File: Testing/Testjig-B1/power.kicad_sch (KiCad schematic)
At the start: 29 parts, among them U1 LM7805_TO220, U2 LM7815_TO220, U3 LM317_TO-220, U4 LM7915_TO220, U5 LM7924_TO220

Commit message: More PSU work
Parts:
- added F1, F2, F3, F5: 100mAT, symbol Device:Fuse
- added F4: 150mAT, symbol Device:Fuse
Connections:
- net +VDC: now also F1.1, F2.1, F3.1; no longer C1.1, C2.1, C3.1, D1.1 (K), D2.1 (K), D3.1 (K), U1.1 (VI), U2.1 (VI), U3.3 (VI)
- net -VDC: now also F4.1, F5.1; no longer C4.2, C5.2, D4.2 (A), D5.2 (A), U4.2 (VI), U5.2 (VI)
- net +6V: now reaches C7.1, D1.2 (A), D11.1 (K), D6.1 (K), R2.1, U3.2 (VO)
- net +5V: now reaches C8.1, D2.2 (A), D7.1 (K), U1.3 (VO)
- net +15V: now reaches C9.1, D3.2 (A), D8.1 (K), U2.3 (VO)
- net -15V: now reaches C10.2, D4.1 (K), D9.2 (A), U4.3 (VO)
- net -24V: now reaches C11.2, D10.2 (A), D5.1 (K), U5.3 (VO)
- new net: C2.1, D2.1 (K), F2.2, U1.1 (VI)
- new net: C1.1, D1.1 (K), F1.2, U3.3 (VI)
- new net: C3.1, D3.1 (K), F3.2, U2.1 (VI)
- new net: C5.2, D5.2 (A), F5.2, U5.2 (VI)
- new net: C4.2, D4.2 (A), F4.2, U4.2 (VI)

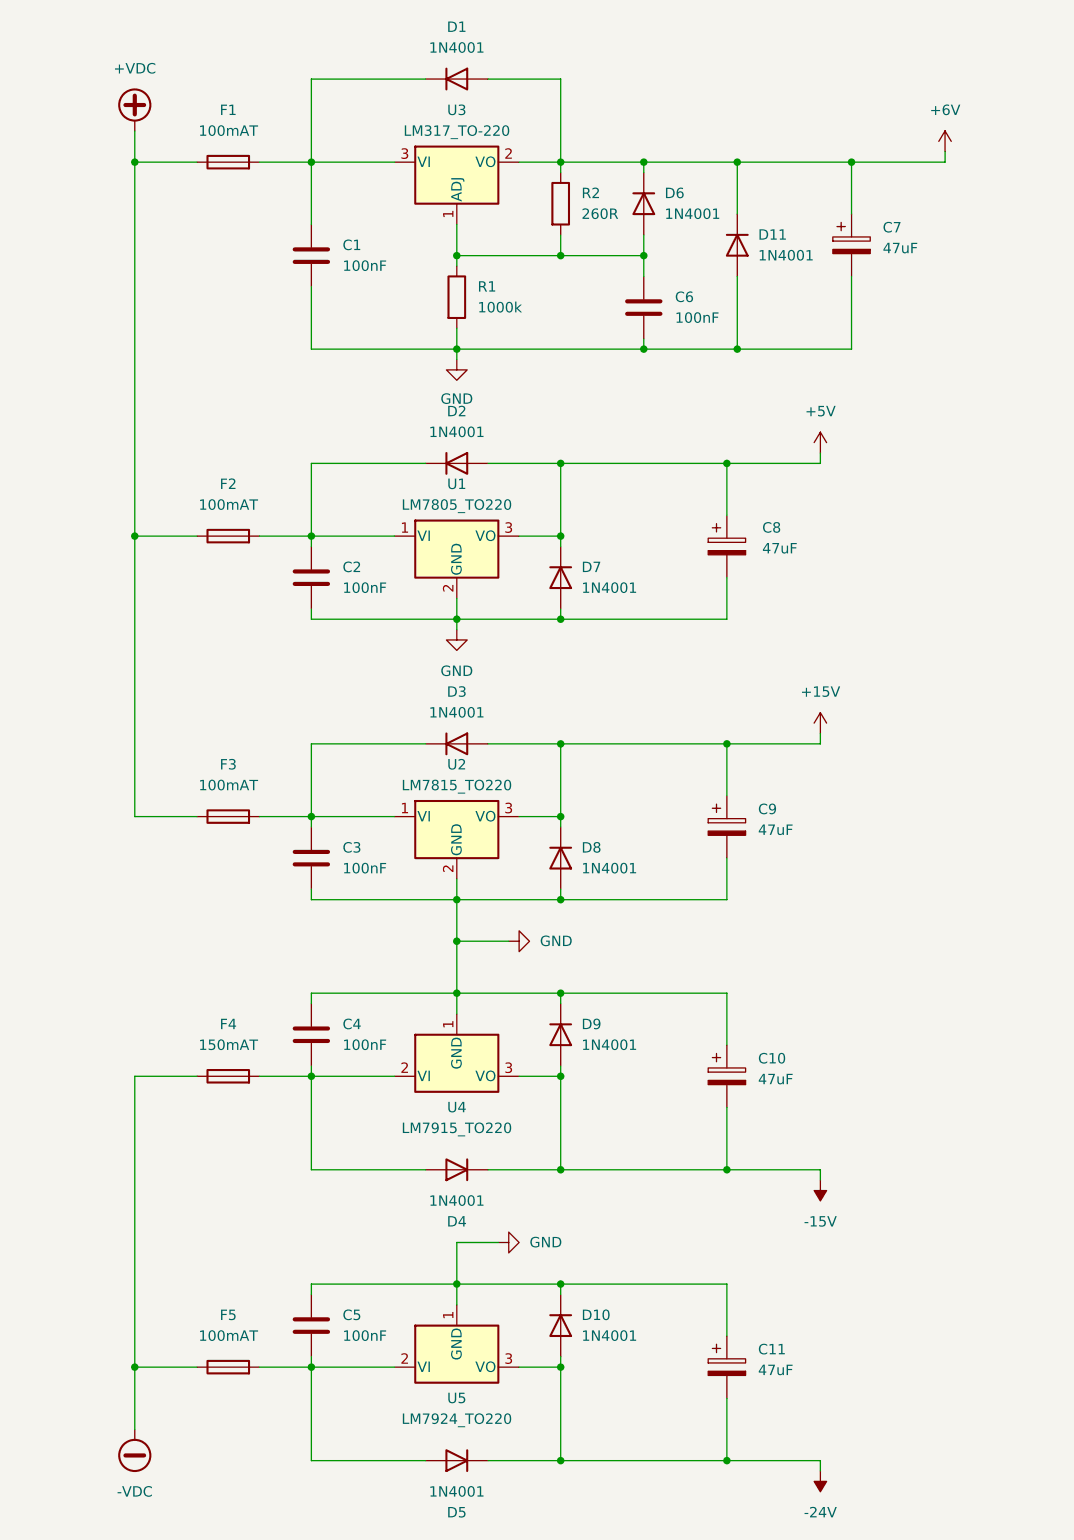
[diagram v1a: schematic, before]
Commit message: First iteration tester design
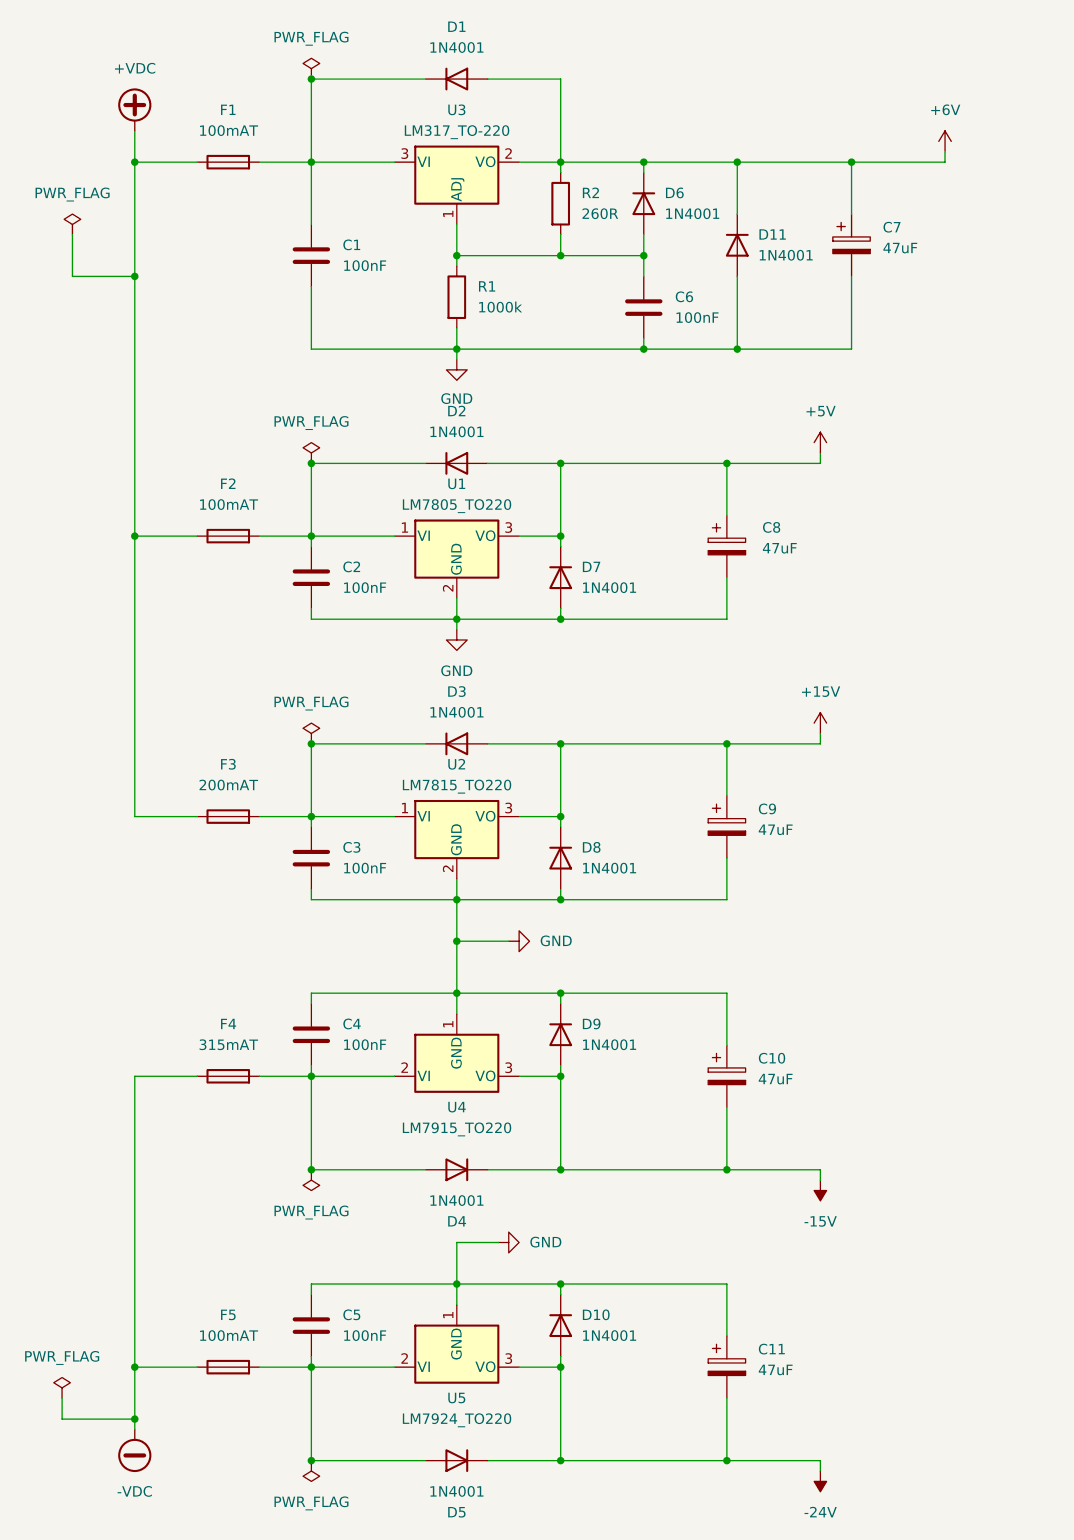
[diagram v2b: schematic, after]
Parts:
- C1, C2, C3, C4, C5, C6: footprint (none) -> Capacitor_SMD:C_0805_2012Metric_Pad1.18x1.45mm_HandSolder
- C10, C11, C7, C8, C9: footprint (none) -> Capacitor_THT:CP_Radial_D6.3mm_P2.50mm
- F1, F2, F5: footprint (none) -> Fuse:Fuseholder_Cylinder-5x20mm_Schurter_0031_8201_Horizontal_Open
- F3: value 100mAT -> 200mAT; footprint (none) -> Fuse:Fuseholder_Cylinder-5x20mm_Schurter_0031_8201_Horizontal_Open
- F4: value 150mAT -> 315mAT; footprint (none) -> Fuse:Fuseholder_Cylinder-5x20mm_Schurter_0031_8201_Horizontal_Open
- R1, R2: footprint (none) -> Resistor_SMD:R_0805_2012Metric

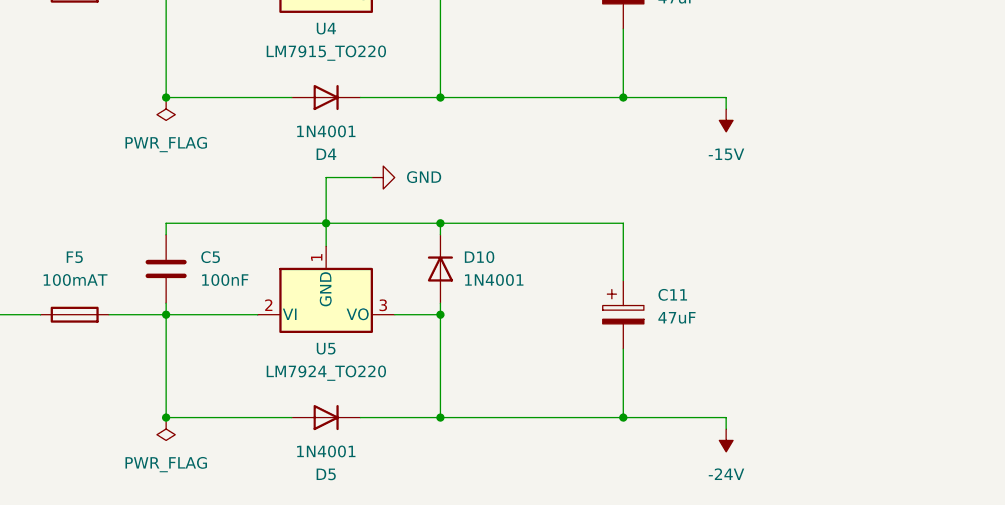
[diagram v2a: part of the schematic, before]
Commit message: Make +24V actually +20V as the UPL does
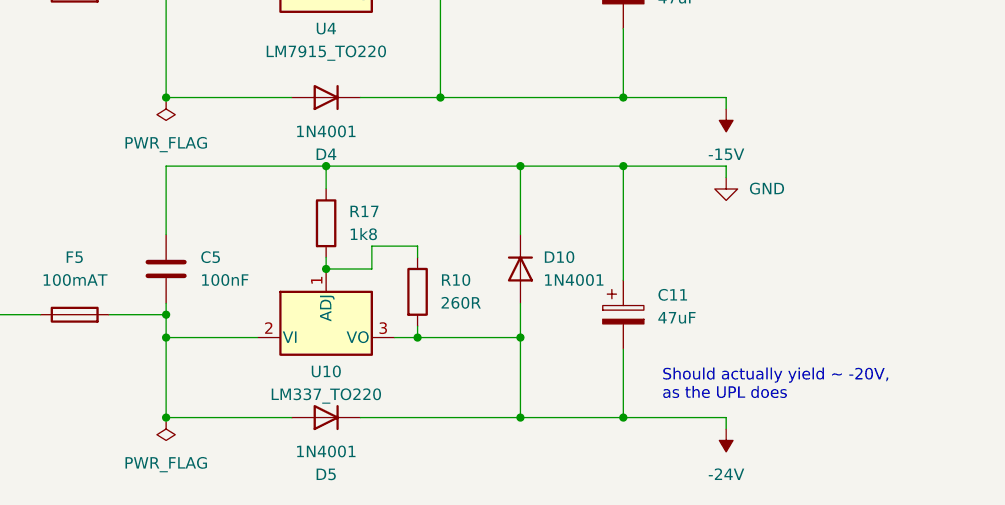
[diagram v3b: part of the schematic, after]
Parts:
- removed U5: LM7924_TO220, Package_TO_SOT_THT:TO-220-3_Vertical, symbol Regulator_Linear:LM7924_TO220
- added R10: 260R, Resistor_SMD:R_0805_2012Metric, symbol Device:R
- added R17: 1k8, Resistor_SMD:R_0805_2012Metric, symbol Device:R
- added U10: LM337_TO220, Package_TO_SOT_THT:TO-220-3_Vertical, symbol Regulator_Linear:LM337_TO220
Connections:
- net -24V: now also R10.2, U10.3 (VO)
- net GND: now also R17.1
- net at C5.2, D5.2 (A), F5.2: now also U10.2 (VI)
- new net: R10.1, R17.2, U10.1 (ADJ)
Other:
- note added: "Should actually yield ~ -20V, as the UPL does"
- moved on the sheet: D10

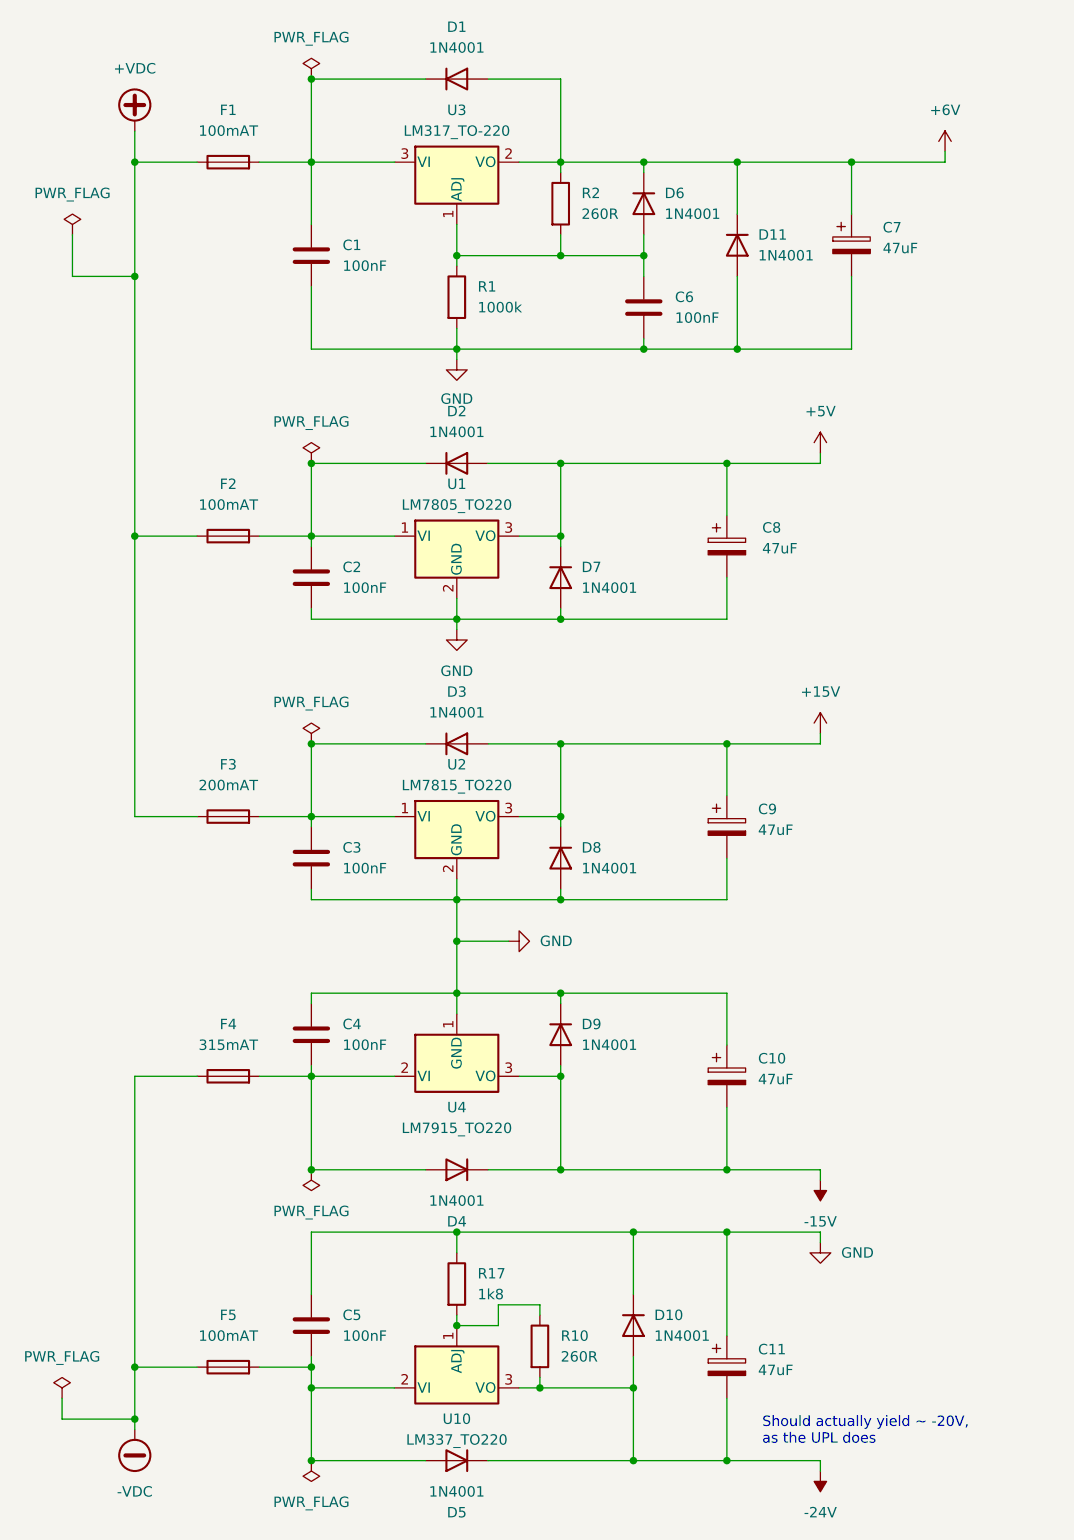
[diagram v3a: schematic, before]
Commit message: Calculate power requirements and heat sinks.
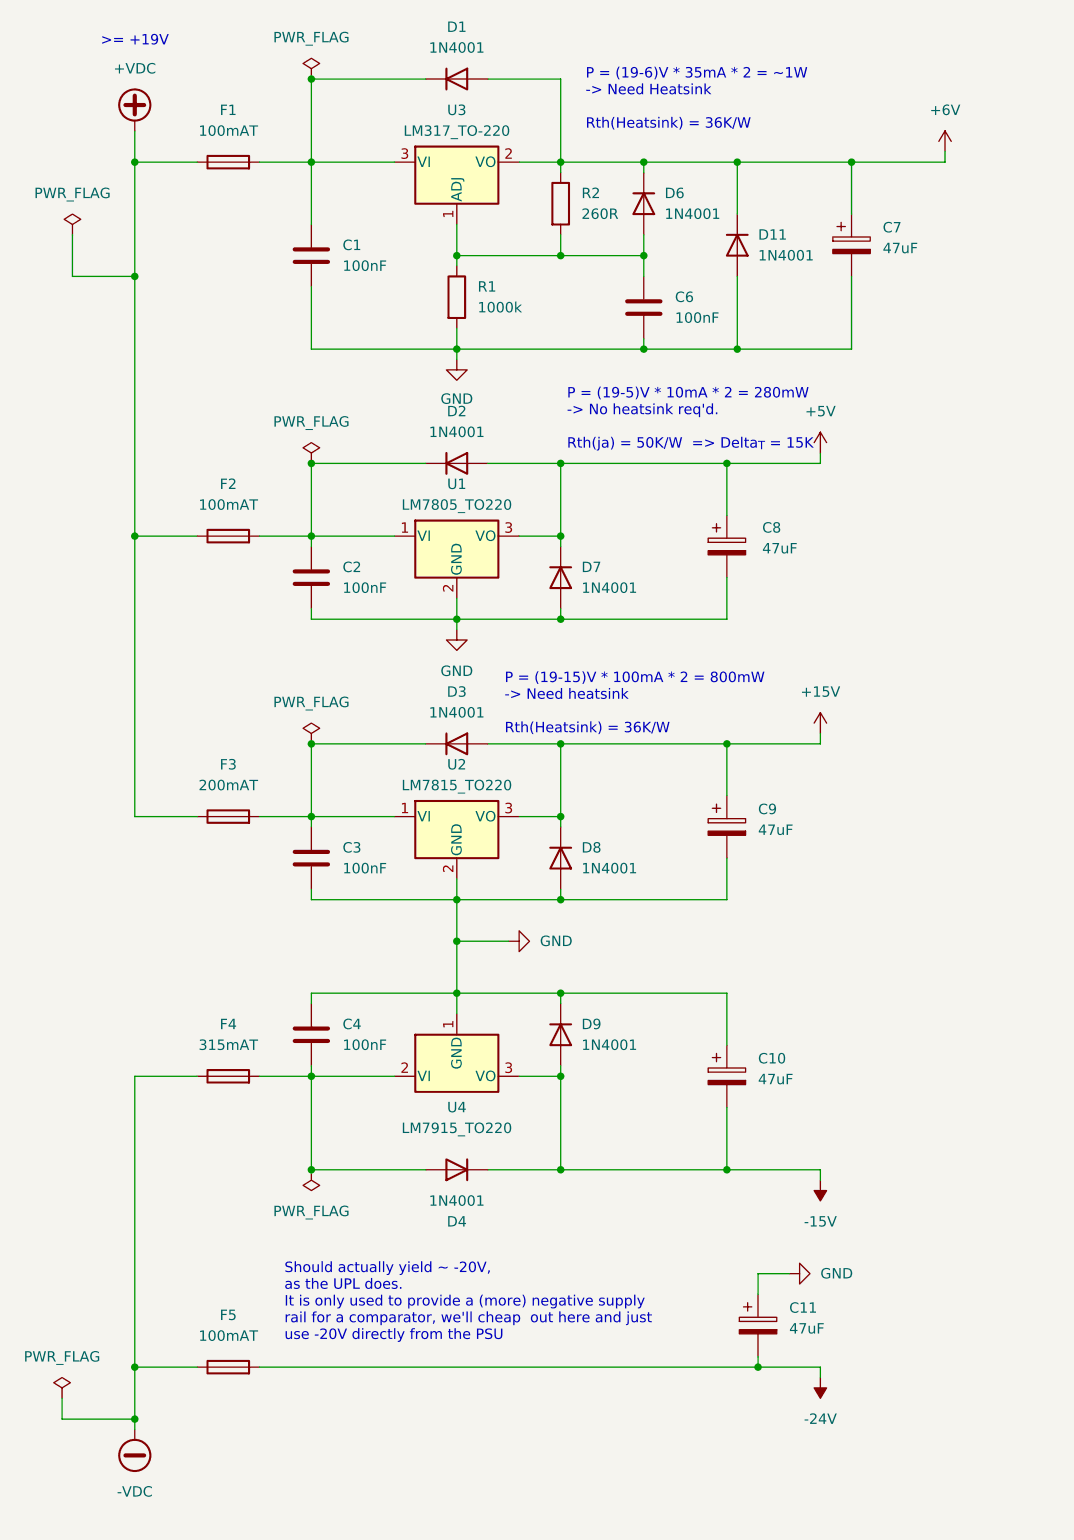
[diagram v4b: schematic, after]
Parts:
- removed C5: 100nF, Capacitor_SMD:C_0805_2012Metric_Pad1.18x1.45mm_HandSolder, symbol Device:C
- removed D10, D5: 1N4001, Diode_THT:D_DO-41_SOD81_P10.16mm_Horizontal, symbol Diode:1N4001
- removed R10: 260R, Resistor_SMD:R_0805_2012Metric, symbol Device:R
- removed R17: 1k8, Resistor_SMD:R_0805_2012Metric, symbol Device:R
- removed U10: LM337_TO220, Package_TO_SOT_THT:TO-220-3_Vertical, symbol Regulator_Linear:LM337_TO220
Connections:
- net -24V: now also F5.2
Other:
- note added: ">= +19V"
- note added: "P = (19-15)V * 100mA * 2 = 800mW -> Need heatsink Rth(Heatsink) = 36K/W"
- note added: "P = (19-5)V * 10mA * 2 = 280mW -> No heatsink req'd. Rth(ja) = 50K/W => Delta_{T} = 15K"
- note added: "P = (19-6)V * 35mA * 2 = ~1W -> Need Heatsink Rth(Heatsink) = 36K/W"
- note added: "Should actually yield ~ -20V, as the UPL does. It is only used to provide a (more) negative supply rail for a comparator, we'll cheap out here and just use -20V directly from the PSU"
- note removed: "Should actually yield ~ -20V, as the UPL does"
- moved on the sheet: C11

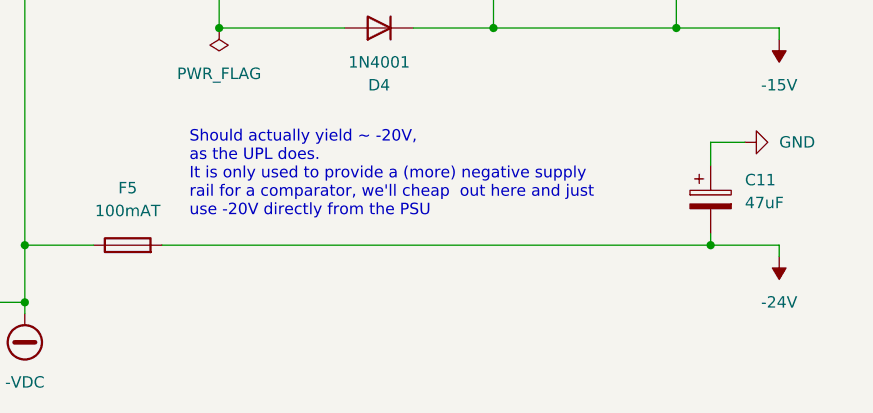
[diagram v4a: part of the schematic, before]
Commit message: Last fixes before production of Rev A.
- Add signal line for SDO1 which had a break in the schematic.
- Route out said signal
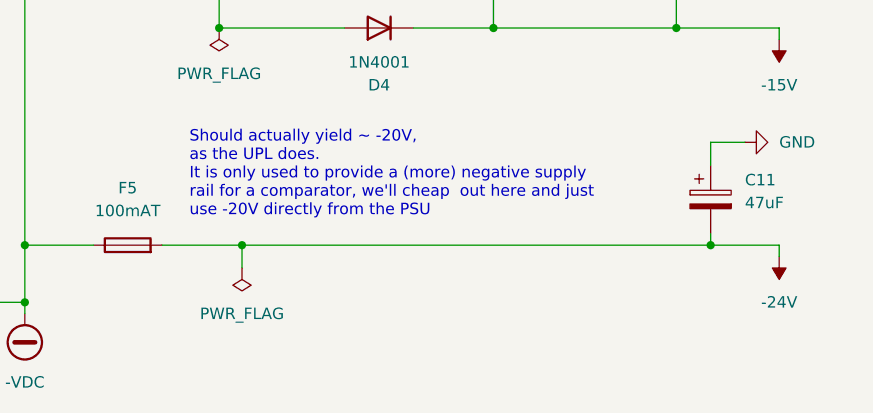
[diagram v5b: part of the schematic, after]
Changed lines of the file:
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@@
+	)
+	(junction
+		(at 60.96 177.8)
+		(diameter 0)
+		(color 0 0 0 0)
 	)
 	(junction
@@
 	(wire
 		(pts
+			(xy 60.96 177.8) (xy 113.03 177.8)
+		)
+		(stroke
+			(width 0)
+			(type default)
+		)
+	)
+	(wire
+		(pts
 			(xy 58.42 76.2) (xy 58.42 67.31)
 		)
@@
 	(wire
 		(pts
-			(xy 52.07 177.8) (xy 113.03 177.8)
+			(xy 52.07 177.8) (xy 60.96 177.8)
 		)
 		(stroke
@@
 		(pts
 			(xy 58.42 142.24) (xy 52.07 142.24)
+		)
+		(stroke
+			(width 0)
+			(type default)
+		)
+	)
+	(wire
+		(pts
+			(xy 60.96 177.8) (xy 60.96 180.34)
 		)
 		(stroke
@@
 				)
 			)
+		)
+	)
+	(symbol
+		(lib_id "power:PWR_FLAG")
+		(at 60.96 180.34 0)
+		(mirror x)
+		(unit 1)
+		(body_style 1)
+		(exclude_from_sim no)
+		(in_bom yes)
+		(on_board yes)
+		(in_pos_files yes)
+		(dnp no)
+		(property "Reference" "#FLG09"
+			(at 60.96 182.245 0)
+			(hide yes)
+			(show_name no)
+			(do_not_autoplace no)
+			(effects
+				(font
+					(size 1.27 1.27)
+				)
+			)
+		)
+		(property "Value" "PWR_FLAG"
+			(at 60.96 185.42 0)
+			(show_name no)
+			(do_not_autoplace no)
+			(effects
+				(font
+					(size 1.27 1.27)
+				)
+			)
+		)
+		(property "Footprint" ""
+			(at 60.96 180.34 0)
+			(hide yes)
+			(show_name no)
+			(do_not_autoplace no)
+			(effects
+				(font
+					(size 1.27 1.27)
+				)
+			)
+		)
+		(property "Datasheet" ""
+			(at 60.96 180.34 0)
+			(hide yes)
+			(show_name no)
+			(do_not_autoplace no)
+			(effects
+				(font
+					(size 1.27 1.27)
+				)
+			)
+		)
+		(property "Description" "Special symbol for telling ERC where power comes from"
+			(at 60.96 180.34 0)
+			(hide yes)
+			(show_name no)
+			(do_not_autoplace no)
+			(effects
+				(font
+					(size 1.27 1.27)
+				)
+			)
+		)
+		(pin "1"
+		)
+		(instances
+			(project "Testjig-B1"
+				(path "/ac0bcd9a-6984-47ed-9080-83e8edfb761b/af35ebb4-6c8a-4e10-a66f-24caa5f171b3"
+					(reference "#FLG09")
+					(unit 1)
+				)
+			)
